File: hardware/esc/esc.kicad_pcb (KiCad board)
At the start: 8 copper layers, 38 x 41.5 mm, 219 parts, among them J1 TO_FC, J10 PHASE_A, J11 PHASE_B, J12 PHASE_C, J13 PHASE_A, J14 PHASE_B, J15 PHASE_C, J2 BAT_IN, J3 BAT_GND, J4 PHASE_A, J5 PHASE_B, J6 PHASE_C, J7 PHASE_A, J8 PHASE_B, J9 PHASE_C, Q1 NVTFWS003N04XMTAG, Q10 NVTFWS003N04XMTAG, Q11 NVTFWS003N04XMTAG, Q12 NVTFWS003N04XMTAG, Q13 NVTFWS003N04XMTAG, Q14 NVTFWS003N04XMTAG, Q15 NVTFWS003N04XMTAG, Q16 NVTFWS003N04XMTAG, Q17 NVTFWS003N04XMTAG, Q18 NVTFWS003N04XMTAG, Q19 NVTFWS003N04XMTAG, Q2 NVTFWS003N04XMTAG, Q20 NVTFWS003N04XMTAG, Q21 NVTFWS003N04XMTAG, Q22 NVTFWS003N04XMTAG, Q23 NVTFWS003N04XMTAG, Q24 NVTFWS003N04XMTAG, Q3 NVTFWS003N04XMTAG, Q4 NVTFWS003N04XMTAG, Q5 NVTFWS003N04XMTAG, Q6 NVTFWS003N04XMTAG, Q7 NVTFWS003N04XMTAG, Q8 NVTFWS003N04XMTAG, Q9 NVTFWS003N04XMTAG, U1 DRV8300DRGER, U10 DRV8300DRGER, U11 STM32G071K8U6, U12 INA180A1, U13 LMR51420YFDDCR, U14 NCP59800BMNADJTAG, U2 STM32G071K8U6, U3 INA180A1, U4 DRV8300DRGER, U5 STM32G071K8U6, U6 INA180A1, U7 DRV8300DRGER, U8 STM32G071K8U6, U9 INA180A1

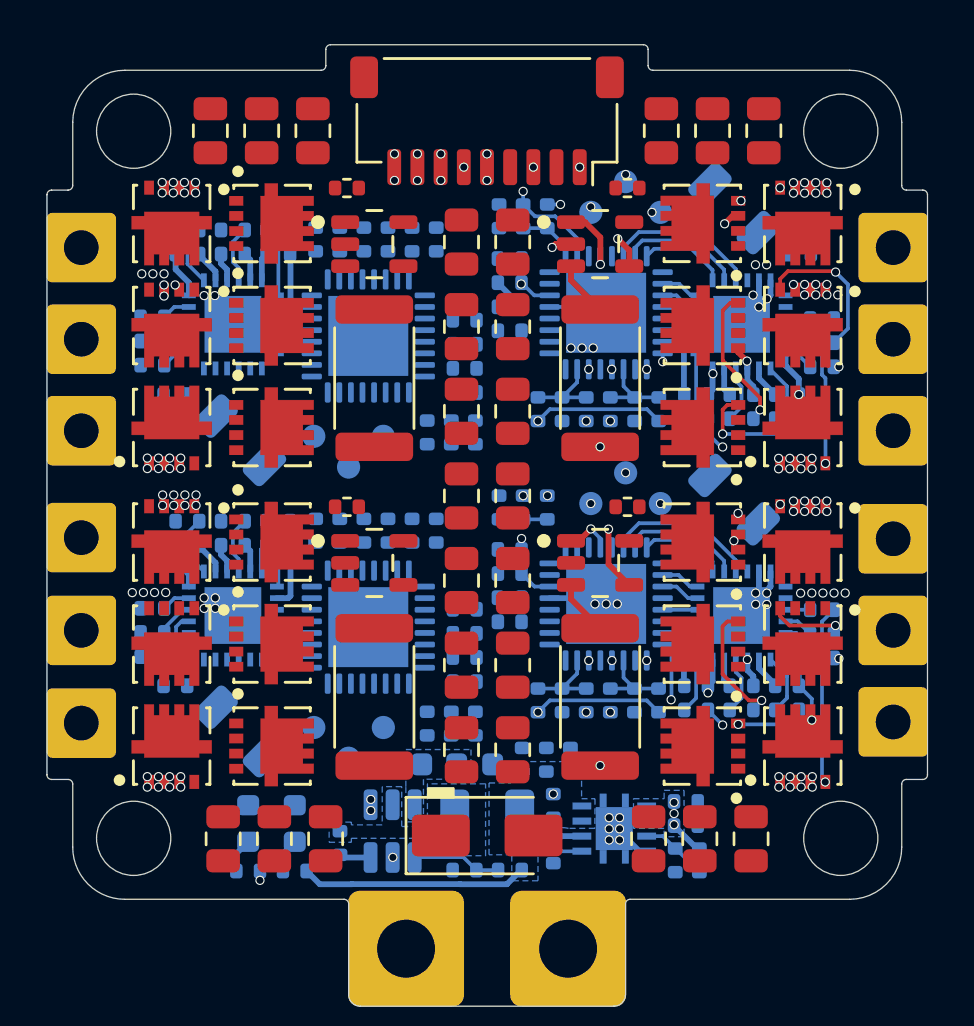
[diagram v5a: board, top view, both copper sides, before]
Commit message: h/feat: 3/4 escs
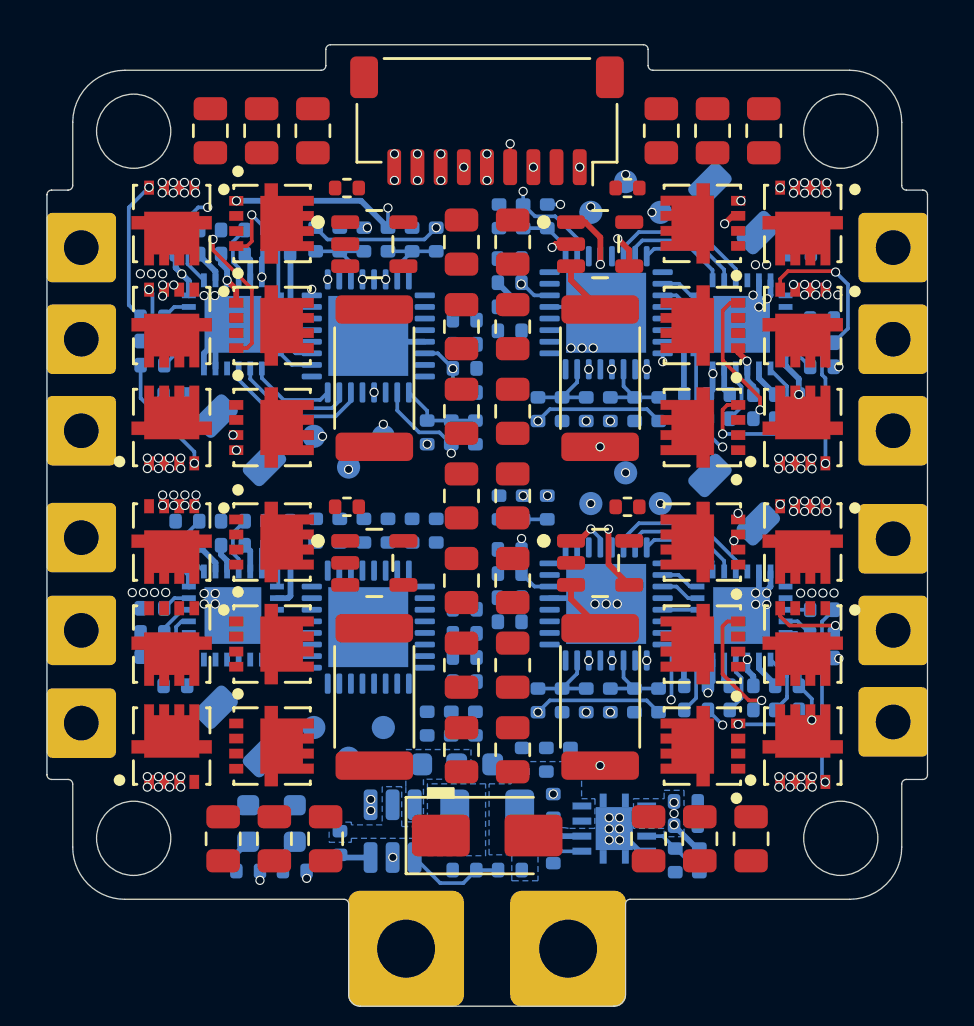
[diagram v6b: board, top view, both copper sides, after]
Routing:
- net /ESC Module 1/VIRTUAL: track 0.00 -> 19.7 mm, vias 0 -> 2
- net /ESC Module 1/PHASE_C: track 2.02 -> 18.9 mm, vias 0 -> 3
- net /ESC Module 1/PHASE_A: track 1.21 -> 16.3 mm, vias 0 -> 3
- net Net-(Q5-G): track 0.00 -> 13.1 mm, vias 0 -> 2
- net /M1: track 0.00 -> 10.5 mm, vias 0 -> 2
- net V_5V: track 13.6 -> 4.17 mm, vias 2 -> 3
- net GND: track 21.2 -> 30.4 mm, vias 120 -> 119
- net /ESC Module 1/nRST: track 0.00 -> 8.94 mm, vias 0 -> 2
- net /ESC Module 1/PHASE_B: track 1.24 -> 9.52 mm, vias 0 -> 2
- net /ESC Module 1/SWCLK: track 0.00 -> 7.77 mm, vias 0 -> 2
- net /ESC Module 1/SWDIO: track 0.00 -> 7.17 mm, vias 0 -> 2
- net /ESC Module 1/LC: track 0.00 -> 6.63 mm
- net Net-(Q3-G): track 0.00 -> 6.49 mm, vias 0 -> 1
- net Net-(Q2-G): track 0.00 -> 6.18 mm, vias 0 -> 1
- net /ESC Module 1/LB: track 0.00 -> 5.32 mm
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
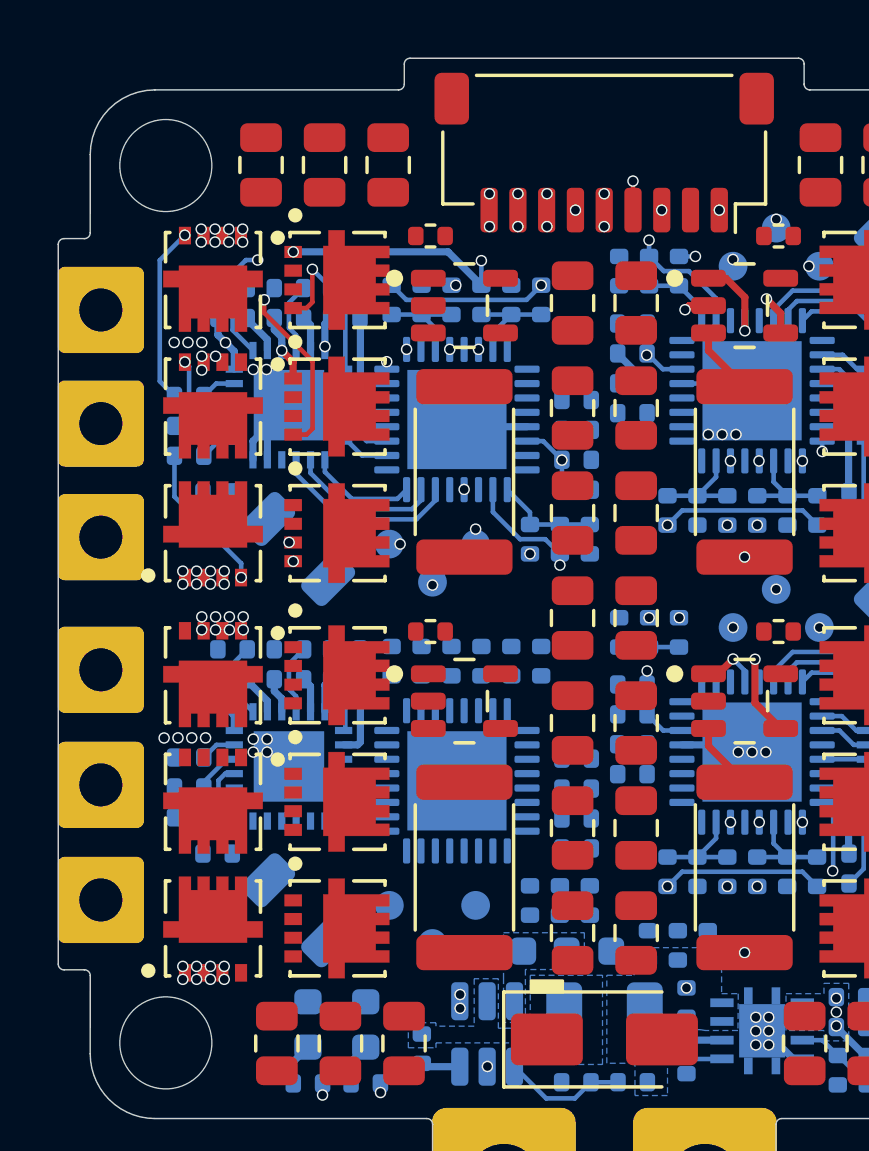
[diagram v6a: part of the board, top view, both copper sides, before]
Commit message: h/feat: 4/4 escs
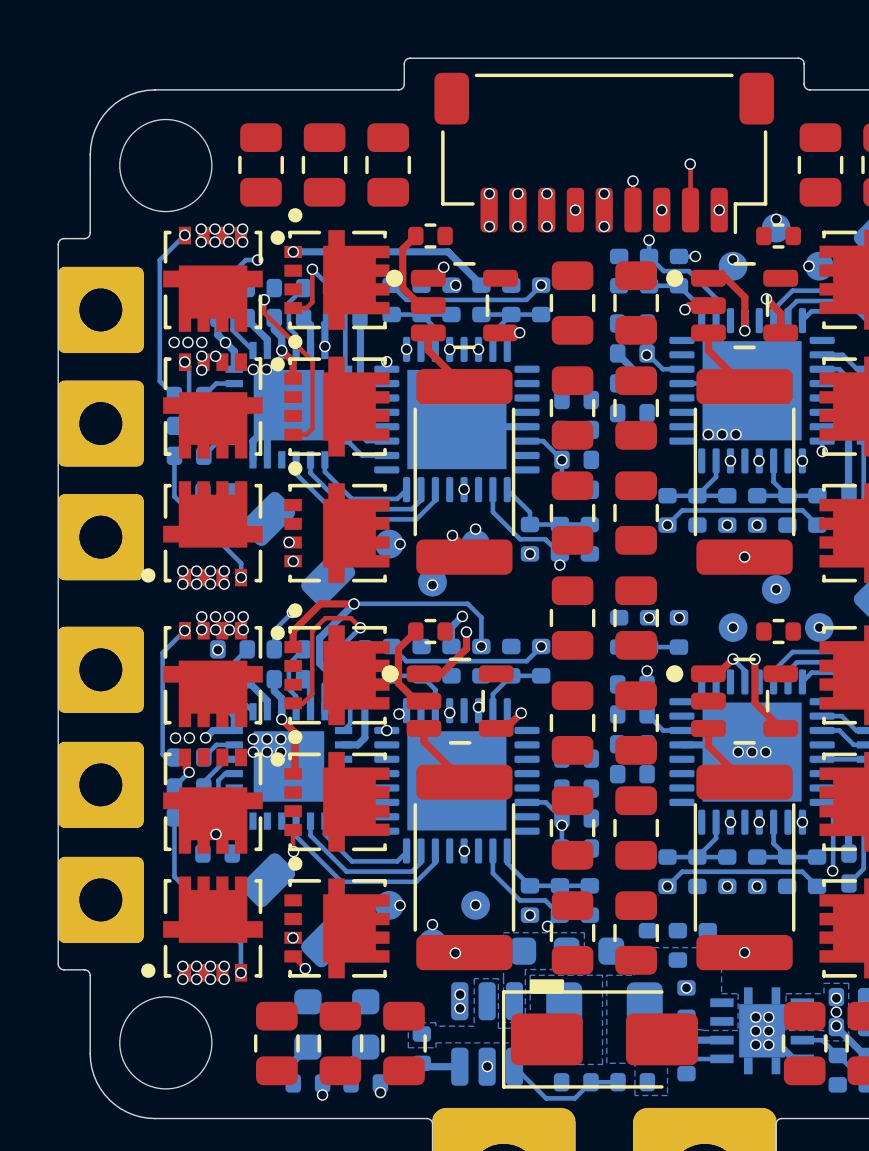
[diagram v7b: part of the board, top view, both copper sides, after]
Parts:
- moved C22 0.17 mm to (157.6, 94.2)
- moved R54 0.17 mm to (157.6, 93.2)
- moved U9 0.15 mm to (161.4, 95.0)
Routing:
- net /M3: track 0.00 -> 27.5 mm, vias 0 -> 2
- net /ESC Module 3/VIRTUAL: track 0.00 -> 19.8 mm, vias 0 -> 2
- net /ESC Module 3/PHASE_C: track 2.02 -> 21.1 mm, vias 0 -> 3
- net Net-(Q15-G): track 0.00 -> 13.0 mm, vias 0 -> 2
- net /ESC Module 3/PHASE_A: track 1.21 -> 13.3 mm, vias 0 -> 2
- net /ESC Module 3/PHASE_B: track 1.24 -> 13.1 mm, vias 0 -> 3
- net Net-(Q13-G): track 0.00 -> 11.1 mm, vias 0 -> 2
- net /ESC Module 3/V_FET: track 0.00 -> 10.7 mm, vias 0 -> 2
- net /ESC Module 3/SNS_CURR: track 0.00 -> 10.1 mm, vias 0 -> 2
- net /ESC Module 1/SNS_CURR: track 0.01 -> 9.99 mm, vias 1 -> 2
- net /ESC Module 3/nRST: track 0.00 -> 9.85 mm, vias 0 -> 2
- net /ESC Module 1/V_FET: track 0.00 -> 9.61 mm, vias 0 -> 2
- net /ESC Module 3/SWCLK: track 0.00 -> 8.07 mm, vias 0 -> 2
- net /ESC Module 1/PHASE_A: track 16.3 -> 8.24 mm, vias 3 -> 2
- net /ESC Module 3/SWDIO: track 0.00 -> 6.65 mm, vias 0 -> 2
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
